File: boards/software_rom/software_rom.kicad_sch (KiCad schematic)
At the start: 19 parts, among them J1 Conn_02x10_Top_Bottom, J2 uart_conn, J3 ICSP, SW1 SW_Push, U1 ATmega328P-P, Y1 16MHz

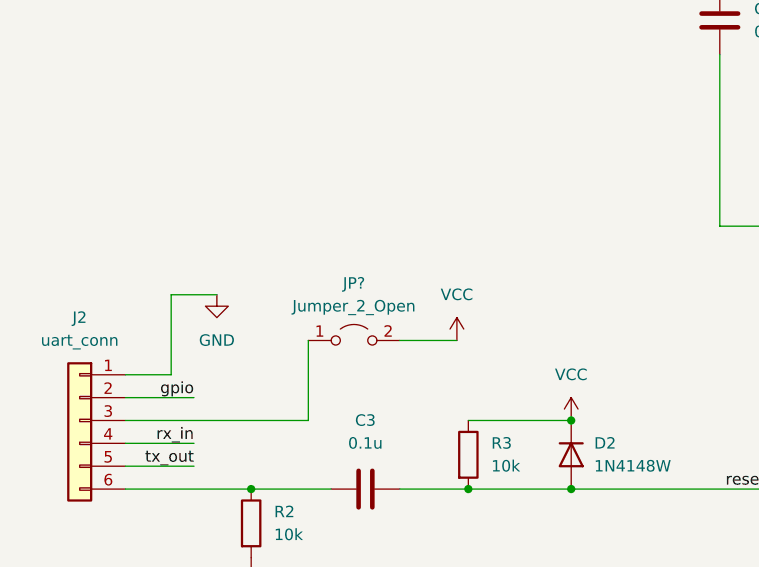
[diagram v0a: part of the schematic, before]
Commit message: software_rom: add board design
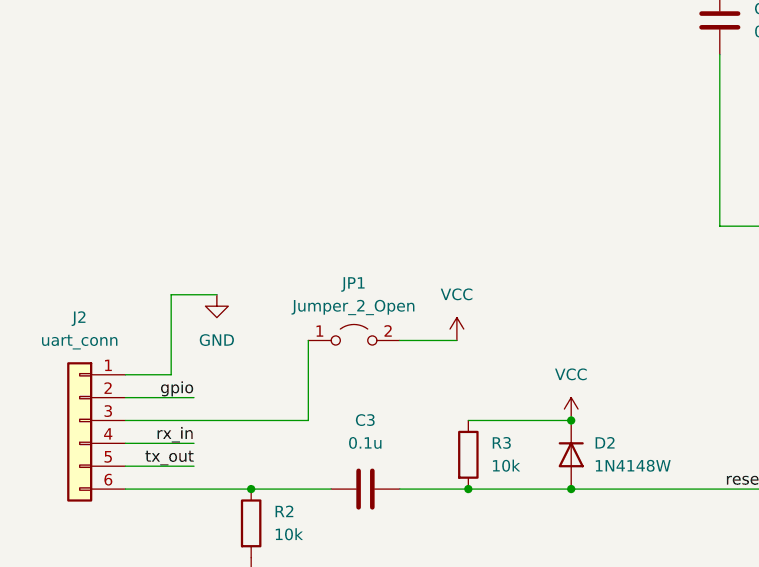
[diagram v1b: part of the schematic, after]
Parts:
- C1, C2, C3, C4, C5: footprint (none) -> Capacitor_SMD:C_0805_2012Metric_Pad1.18x1.45mm_HandSolder
- D1: footprint (none) -> LED_SMD:LED_0805_2012Metric_Pad1.15x1.40mm_HandSolder
- D2: footprint (none) -> Diode_SMD:D_SOD-123
- J2: footprint (none) -> Connector_PinHeader_2.54mm:PinHeader_1x06_P2.54mm_Vertical
- J3: footprint (none) -> Connector_PinHeader_2.54mm:PinHeader_2x03_P2.54mm_Vertical
- JP1: renamed from JP?; footprint (none) -> Connector_PinHeader_2.54mm:PinHeader_1x02_P2.54mm_Vertical
- R1, R2, R3, R4, R5: footprint (none) -> Resistor_SMD:R_0805_2012Metric_Pad1.20x1.40mm_HandSolder
- SW1: footprint (none) -> Button_Switch_THT:SW_PUSH_6mm_H7.3mm
- U1: footprint Package_DIP:DIP-28_W7.62mm -> PrjLibrary_ClockReset:DIP-28_W7.62mm-D1mm
- Y1: footprint (none) -> Crystal:Crystal_HC49-4H_Vertical

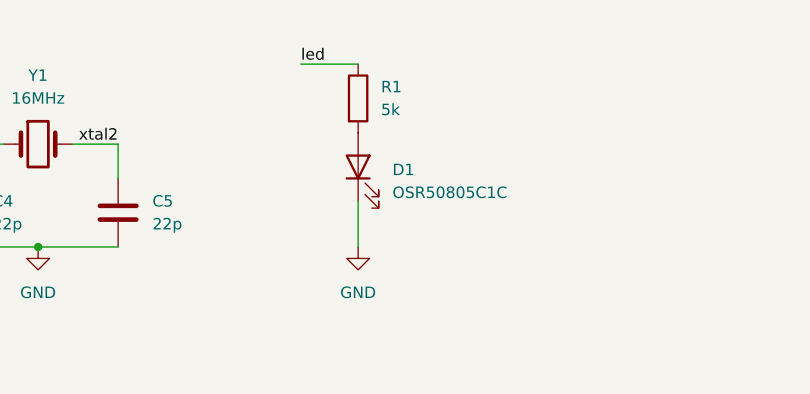
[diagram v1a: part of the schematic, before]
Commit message: change values according to actual parts
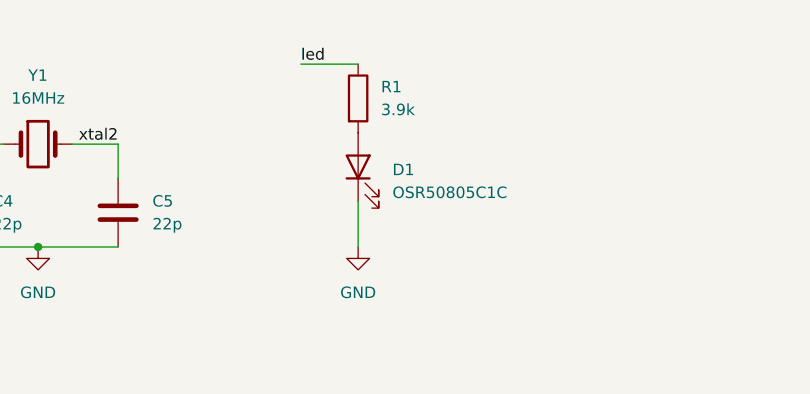
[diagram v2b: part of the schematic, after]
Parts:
- R1: value 5k -> 3.9k
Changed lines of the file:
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@@
       (effects (font (size 1.27 1.27)) (justify left))
     )
-    (property "Value" "5k" (id 1) (at 121.92 31.7499 0)
+    (property "Value" "3.9k" (id 1) (at 121.92 31.7499 0)
       (effects (font (size 1.27 1.27)) (justify left))
     )
@@
     )
     (path "/4155505f-3687-467b-8149-9afc3d422f5e"
-      (reference "R1") (unit 1) (value "5k") (footprint "Resistor_SMD:R_0805_2012Metric_Pad1.20x1.40mm_HandSolder")
+      (reference "R1") (unit 1) (value "3.9k") (footprint "Resistor_SMD:R_0805_2012Metric_Pad1.20x1.40mm_HandSolder")
     )
     (path "/27c8c828-a053-4c69-b7ae-c7f1bafdd083"

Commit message: unify libraries
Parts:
- J1: footprint PrjLibrary_MainBoard:PinHeader_2x10_P2.54mm_Vertical_Top_Bottom -> ModifiedKiCadLibrary:PinHeader_2x10_P2.54mm_Vertical_Top_Bottom
- U1: footprint PrjLibrary_ClockReset:DIP-28_W7.62mm-D1mm -> ModifiedKiCadLibrary:DIP-28_W7.62mm-D1mm
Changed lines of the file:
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@@
     (property "Reference" "J1" (id 0) (at 232.41 22.86 0))
     (property "Value" "Conn_02x10_Top_Bottom" (id 1) (at 232.41 25.4 0))
-    (property "Footprint" "PrjLibrary_MainBoard:PinHeader_2x10_P2.54mm_Vertical_Top_Bottom" (id 2) (at 231.14 39.37 0)
+    (property "Footprint" "ModifiedKiCadLibrary:PinHeader_2x10_P2.54mm_Vertical_Top_Bottom" (id 2) (at 231.14 39.37 0)
       (effects (font (size 1.27 1.27)) hide)
     )
@@
     (property "Reference" "U1" (id 0) (at 114.3 78.74 0))
     (property "Value" "ATmega328P-P" (id 1) (at 114.3 81.28 0))
-    (property "Footprint" "PrjLibrary_ClockReset:DIP-28_W7.62mm-D1mm" (id 2) (at 135.89 115.57 0)
+    (property "Footprint" "ModifiedKiCadLibrary:DIP-28_W7.62mm-D1mm" (id 2) (at 135.89 115.57 0)
       (effects (font (size 1.27 1.27) italic) hide)
     )
@@
     )
     (path "/e7a553dc-6b20-4896-bb62-ac76a417710b"
-      (reference "J1") (unit 1) (value "Conn_02x10_Top_Bottom") (footprint "PrjLibrary_MainBoard:PinHeader_2x10_P2.54mm_Vertical_Top_Bottom")
+      (reference "J1") (unit 1) (value "Conn_02x10_Top_Bottom") (footprint "ModifiedKiCadLibrary:PinHeader_2x10_P2.54mm_Vertical_Top_Bottom")
     )
     (path "/15f9ce5c-444b-4b49-9e20-44109e09dae0"
@@
     )
     (path "/fa74e58b-1d1f-4c19-a9e0-9a5b12093d6c"
-      (reference "U1") (unit 1) (value "ATmega328P-P") (footprint "PrjLibrary_ClockReset:DIP-28_W7.62mm-D1mm")
+      (reference "U1") (unit 1) (value "ATmega328P-P") (footprint "ModifiedKiCadLibrary:DIP-28_W7.62mm-D1mm")
     )
     (path "/1a6fe569-c5e5-4a21-a4ea-d60011b774d2"
